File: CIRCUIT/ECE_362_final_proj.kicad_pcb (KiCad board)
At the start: 2 copper layers, 90.1 x 75.2 mm, 27 parts, among them J1 Conn_01x01_Pin, J2 Conn_01x01_Pin, J3 Conn_01x28_Socket, J4 Conn_01x28_Socket, SW2 BUTTON_MODE, SW4 BUTTON_CAPTURE, U1 TL084

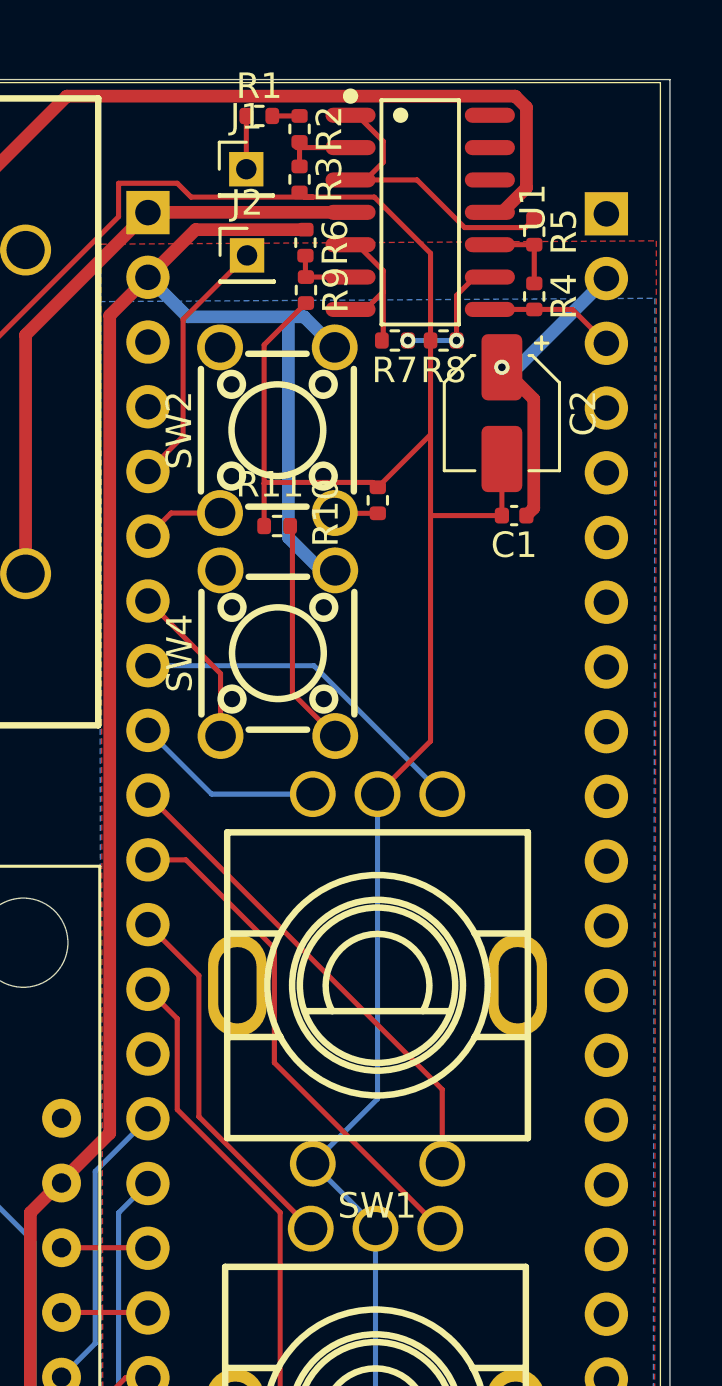
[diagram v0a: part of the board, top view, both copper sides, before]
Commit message: adjusted silkscreen
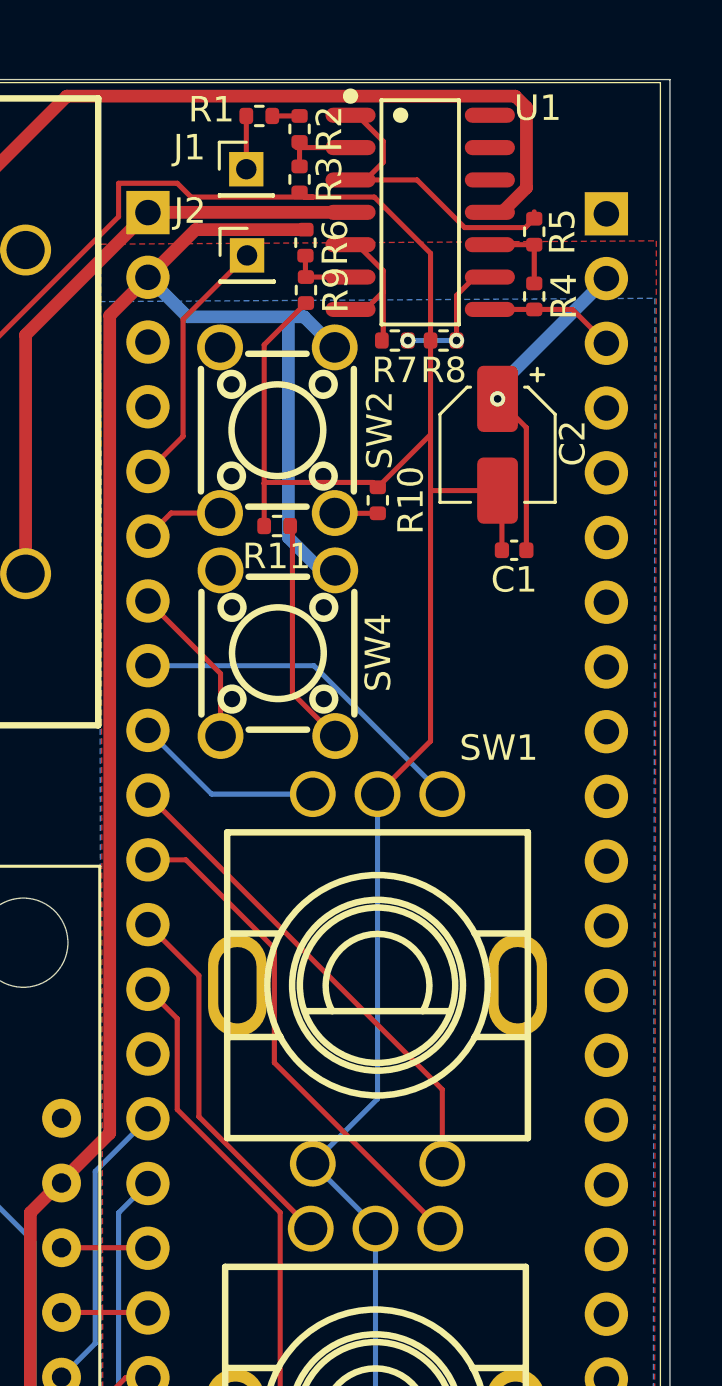
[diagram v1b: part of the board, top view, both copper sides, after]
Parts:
- moved C1 1.36 mm to (15.5, 19.7)
- moved C2 1.25 mm to (14.9, 15.6)
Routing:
- net +3.3V: track 94.1 -> 95.0 mm
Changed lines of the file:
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@@
 		(at 10.18 36.51 180)
 		(property "Reference" "SW1"
-			(at 0.014966 -8.905433 0)
+			(at -4.76 9.06 0)
 			(layer "F.SilkS")
 			(effects
@@
 		(tags "resistor")
 		(property "Reference" "R10"
-			(at -0.488 -2.038 90)
+			(at 0 1.3 90)
 			(layer "F.SilkS")
 			(effects
@@
 		(at 6.25 14.98 90)
 		(property "Reference" "SW2"
-			(at 0 -3.85 90)
+			(at 0 4.02 90)
 			(layer "F.SilkS")
 			(effects
@@
 	(footprint "Capacitor_SMD:C_0402_1005Metric"
 		(layer "F.Cu")
-		(at 15.54 18.33 180)
+		(at 15.54 19.69 180)
 		(descr "Capacitor SMD 0402 (1005 Metric), square (rectangular) end terminal, IPC_7351 nominal, (Body size source: IPC-SM-782 page 76, https://www.pcb-3d.com/wordpress/wp-content/uploads/ipc-sm-782a_amendment_1_and_2.pdf), generated with kicad-footprint-generator")
 		(tags "capacitor")
@@
 		(tags "resistor")
 		(property "Reference" "R5"
-			(at 0 -1.17 90)
+			(at 0 -1.11 270)
 			(layer "F.SilkS")
 			(effects
@@
 		(tags "resistor")
 		(property "Reference" "R11"
-			(at 0.282 1.622 0)
+			(at 0.02 -1.19 0)
 			(layer "F.SilkS")
 			(effects
@@
 		(tags "resistor")
 		(property "Reference" "R1"
-			(at 0 -1.17 0)
+			(at -1.88 -0.248375 0)
 			(layer "F.SilkS")
 			(effects
@@
 		(tags "Through hole pin header THT 1x01 2.00mm single row")
 		(property "Reference" "J1"
-			(at 0 -2.06 0)
+			(at -2.23 -0.848375 0)
 			(layer "F.SilkS")
 			(effects
@@
 		(at 6.27 23.73 90)
 		(property "Reference" "SW4"
-			(at 0 -3.85 90)
+			(at 0.02 3.94 90)
 			(layer "F.SilkS")
 			(effects
@@
 		(at 11.854 6.43 -90)
 		(property "Reference" "U1"
-			(at -0.191625 -4.41775 90)
+			(at -4.09 -4.616 180)
 			(layer "F.SilkS")
 			(effects
@@
 		(tags "Through hole pin header THT 1x01 2.00mm single row")
 		(property "Reference" "J2"
-			(at 0 -2.06 0)
+			(at -2.24 -1.74 0)
 			(layer "F.SilkS")
 			(effects
@@
 	(footprint "Capacitor_SMD:CP_Elec_4x4.5"
 		(layer "F.Cu")
-		(at 15.06 14.31 -90)
+		(at 14.89 15.55 -90)
 		(descr "SMD capacitor, aluminum electrolytic, Nichicon, 4.0x4.5mm")
 		(tags "capacitor electrolytic")
 		(property "Reference" "C2"
-			(at 0 -3.2 90)
+			(at -0.06 -2.95 90)
 			(layer "F.SilkS")
 			(effects
@@
 		(tags "Through hole socket strip THT 1x28 2.54mm single row")
 		(property "Reference" "J4"
-			(at 0 2.77 0)
+			(at 0.02 2.66 180)
 			(layer "B.SilkS")
 			(effects
@@
 	)
 	(segment
-		(start 16.02 18.33)
-		(end 16.311 18.039)
+		(start -3.443 45.683)
+		(end -2.23 44.47)
 		(width 0.5)
 		(layer "F.Cu")
@@
 	)
 	(segment
-		(start -3.443 45.683)
-		(end -2.23 44.47)
-		(width 0.5)
+		(start 16.02 14.88)
+		(end 14.89 13.75)
+		(width 0.2)
 		(layer "F.Cu")
 		(net 1)
 	)
 	(segment
-		(start 16.311 18.039)
-		(end 16.311 13.761)
-		(width 0.5)
+		(start 16.02 19.69)
+		(end 16.02 14.88)
+		(width 0.2)
 		(layer "F.Cu")
 		(net 1)
@@
 	)
 	(segment
-		(start 16.311 13.761)
-		(end 15.06 12.51)
-		(width 0.5)
-		(layer "F.Cu")
-		(net 1)
-	)
-	(segment
 		(start -3.443 61.037)
 		(end -3.443 45.683)
@@
 	)
 	(via
-		(at 15.06 12.51)
+		(at 14.89 13.75)
 		(size 0.6)
 		(drill 0.3)
@@
 	)
 	(segment
-		(start 19.16 9.03)
-		(end 15.68 12.51)
+		(start 14.89 13.3)
+		(end 14.89 13.75)
 		(width 0.5)
 		(layer "B.Cu")
@@
 	)
 	(segment
-		(start 15.68 12.51)
-		(end 15.06 12.51)
-		(width 0.2)
+		(start 19.16 9.03)
+		(end 14.89 13.3)
+		(width 0.5)
 		(layer "B.Cu")
 		(net 1)
@@
 	)
 	(segment
+		(start 12.26 17.33)
+		(end 12.26 27.18)
+		(width 0.2)
+		(layer "F.Cu")
+		(net 67)
+	)
+	(segment
+		(start 15.06 19.69)
+		(end 15.06 17.52)
+		(width 0.2)
+		(layer "F.Cu")
+		(net 67)
+	)
+	(segment
 		(start 12.26 8.037343)
 		(end 12.26 11.46)
@@
 	)
 	(segment
+		(start 14.89 17.35)
+		(end 12.28 17.35)
+		(width 0.2)
+		(layer "F.Cu")
+		(net 67)
+	)
+	(segment
 		(start -0.811 61.169)
 		(end 7.201 61.169)
@@
 	(segment
 		(start 12.26 11.46)
-		(end 12.26 27.18)
+		(end 12.26 17.33)
 		(width 0.2)
 		(layer "F.Cu")
@@
 	)
 	(segment
-		(start 15.06 18.33)
-		(end 15.06 16.11)
-		(width 0.2)
-		(layer "F.Cu")
-		(net 67)
-	)
-	(segment
-		(start 12.29 18.33)
-		(end 12.26 18.3)
-		(width 0.2)
-		(layer "F.Cu")
-		(net 67)
-	)
-	(segment
 		(start 7.12 5.648375)
 		(end 7.303125 5.8315)
@@
 		(width 0.2)
 		(layer "F.Cu")
-		(net 67)
-	)
-	(segment
-		(start 15.06 18.33)
-		(end 12.29 18.33)
-		(width 0.2)
-		(layer "F.Cu")

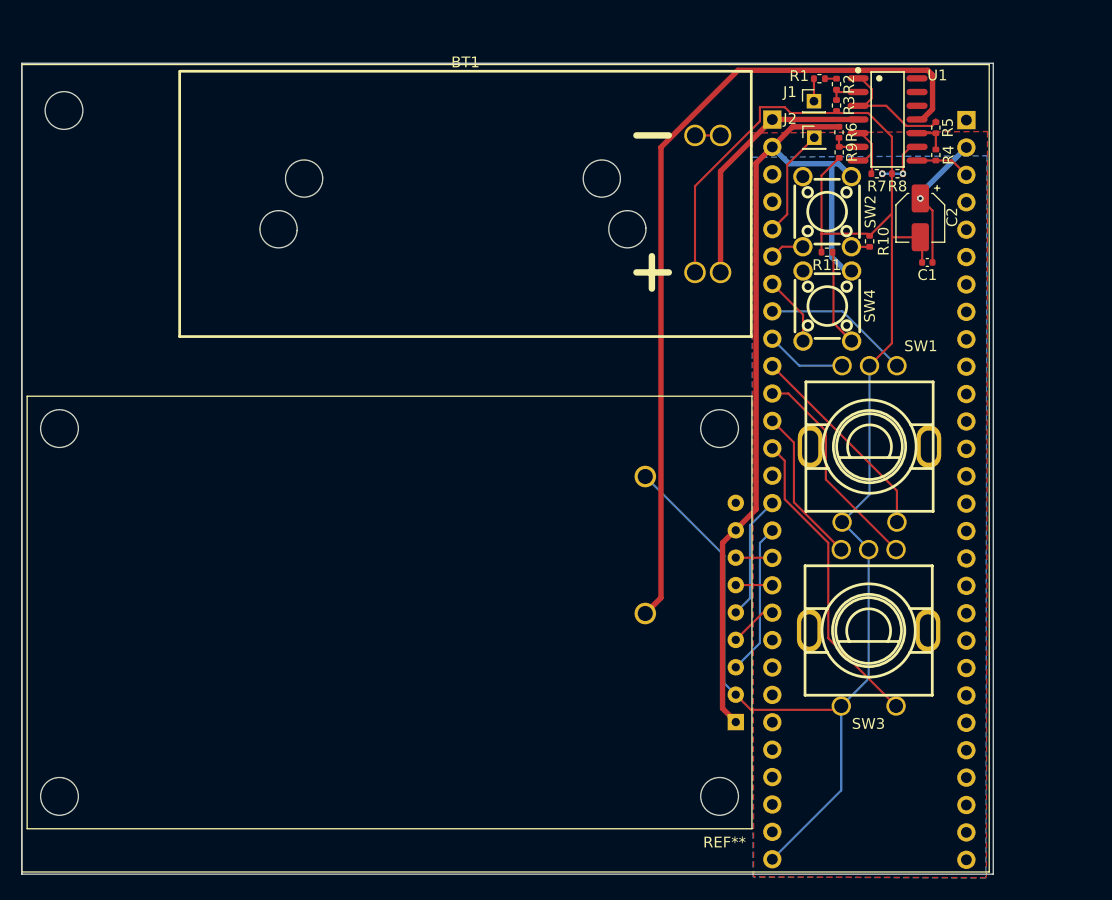
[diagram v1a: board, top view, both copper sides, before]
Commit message: adjusted signal window size
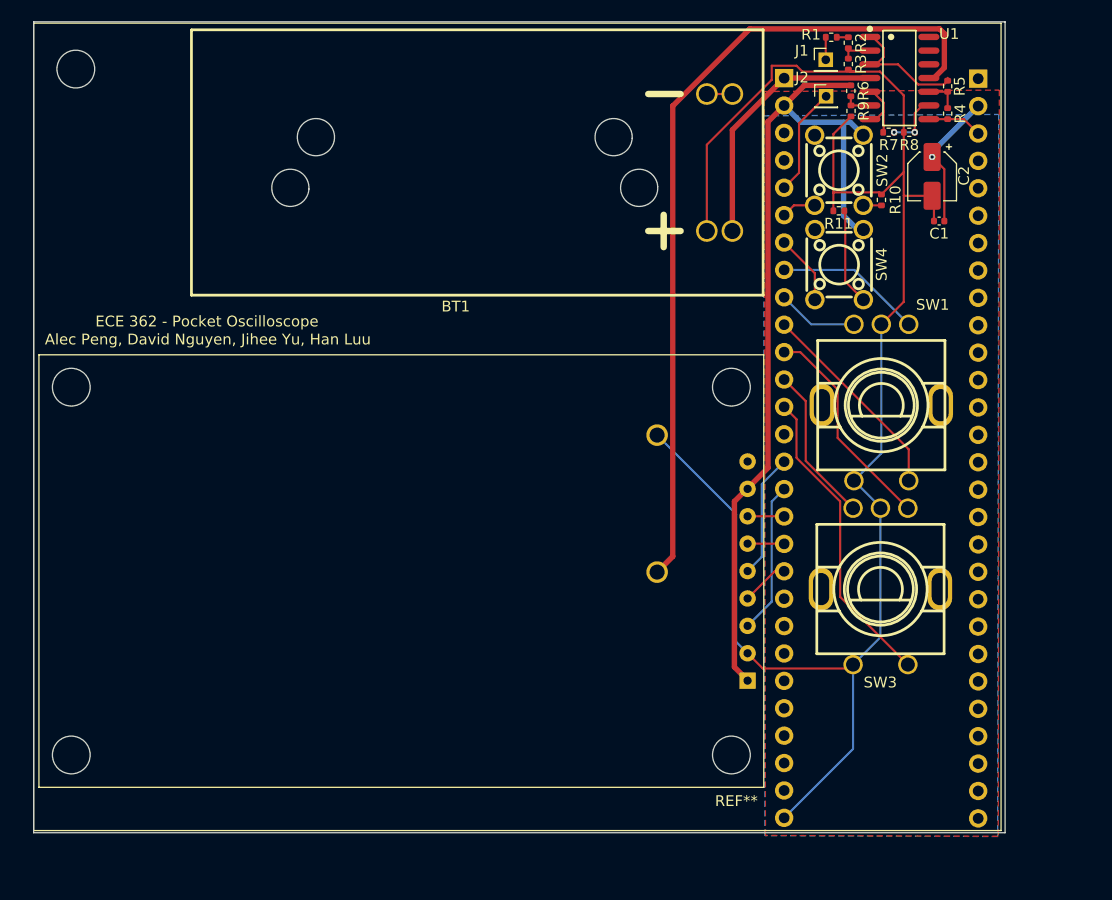
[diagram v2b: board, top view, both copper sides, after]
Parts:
- moved REF** 3.99 mm to (0.38, 68.3)
- moved SW3 3.99 mm to (11.2, 49.7)
- moved C1 3.99 mm to (16.6, 15.8)
- moved R4 3.99 mm to (17.4, 5.89)
- moved R5 3.99 mm to (17.4, 3.35)
- moved R7 3.99 mm to (12.0, 7.62)
- moved R8 3.99 mm to (13.9, 7.62)
- moved R9 3.99 mm to (8.46, 5.64)
- moved J3 3.99 mm to (2.27, 2.60)
- moved J4 3.99 mm to (20.3, 2.65)
- moved R6 3.99 mm to (8.45, 3.78)
- moved ? 3.99 mm to (-63.4, 1.76)
- moved BT1 3.99 mm to (-2.54, 10.4)
- moved BT2 3.99 mm to (-4.91, 10.4)
- moved C2 3.99 mm to (16.0, 11.7)
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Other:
- board text added: "Alec Peng, David Nguyen, Jihee Yu, Han Luu"
- board text added: "ECE 362 - Pocket Oscilloscope"

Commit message: PCB DONE
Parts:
- added U_Switch: SW-TH_SSSS222700, DPDT_switch:SW-TH_SSSS222700, F.Cu at (-0.23, 27.2)
- moved J2 8.20 mm to (14.0, 6.62)
- moved ? 8.03 mm to (-55.5, 3.41)
- moved BT2 8.03 mm to (2.96, 12.1)
- moved C2 8.03 mm to (23.8, 13.4)
- moved J1 8.03 mm to (14.0, 2.55)
- moved R1 8.03 mm to (14.5, 0.46)
- moved R10 8.03 mm to (19.1, 15.5)
- moved R2 8.03 mm to (16.1, 0.97)
- moved R3 8.03 mm to (16.1, 2.95)
- moved R4 8.03 mm to (25.3, 7.54)
- moved R5 8.03 mm to (25.3, 5.00)
- moved R6 8.03 mm to (16.3, 5.43)
- moved R9 8.03 mm to (16.3, 7.29)
- moved SW3 8.03 mm to (19.1, 51.4)
- moved SW4 8.03 mm to (15.2, 21.5)
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- gave numbers to parts that had none: 1
- renumbered REF** to U2
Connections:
- BT1 pad 2: +BATT -> BT1+
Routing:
- net GND: track 161.5 -> 183.3 mm
- net BT1+: track 0.00 -> 16.5 mm
- net +BATT: track 24.1 -> 34.8 mm
- net -BATT: track 77.1 -> 86.5 mm
- net /GPIO2: track 10.2 -> 9.48 mm
- net +3.3V: track 95.0 -> 94.5 mm, vias 1 -> 0
- net /GPIO47_ADC7: track 5.12 -> 4.66 mm, vias 0 -> 1
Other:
- board size 90.1 x 75.2 mm -> 90.5 x 76.1 mm

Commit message: final circuit
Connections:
- BATT3 pad 2: -BATT -> BAT3
- U_Switch pad 2: GND -> BT1+
- U_Switch pad 4: BT1+ -> -BATT
- U_Switch pad 5: -BATT -> BAT3
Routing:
- net -BATT: track 86.5 -> 60.4 mm
- net BAT3: track 0.00 -> 22.5 mm
- net GND: track 183.3 -> 162.9 mm
- net BT1+: track 16.5 -> 9.45 mm
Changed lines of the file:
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@@
 	(net 74 "BT1_GND")
 	(net 75 "BT1+")
+	(net 76 "BAT3")
 	(footprint "Rotary_Encoder_EC11E18244A5:SW-TH_EC11E18244A5"
 		(layer "F.Cu")
@@
 			(layers "*.Cu" "*.Mask")
 			(remove_unused_layers no)
-			(net 67 "GND")
+			(net 75 "BT1+")
 			(thermal_bridge_angle 90)
 		)
@@
 			(layers "*.Cu" "*.Mask")
 			(remove_unused_layers no)
-			(net 75 "BT1+")
+			(net 66 "-BATT")
 			(thermal_bridge_angle 90)
 		)
@@
 			(layers "*.Cu" "*.Mask")
 			(remove_unused_layers no)
-			(net 66 "-BATT")
+			(net 76 "BAT3")
 			(thermal_bridge_angle 90)
 		)
@@
 			(layers "*.Cu" "*.Mask")
 			(remove_unused_layers no)
-			(net 66 "-BATT")
+			(net 76 "BAT3")
 			(thermal_bridge_angle 90)
 		)
@@
 	)
 	(segment
-		(start -3.306892 30.1678)
-		(end -5.786307 27.688385)
-		(width 0.5)
-		(layer "F.Cu")
-		(net 66)
-	)
-	(segment
-		(start -0.228 28.8668)
-		(end 0.622 29.7168)
+		(start -3.946415 27.688385)
+		(end -2.768 28.8668)
 		(width 0.5)
 		(layer "F.Cu")
@@
 	)
 	(segment
-		(start 0.622 47.7685)
-		(end -1.6515 50.042)
-		(width 0.5)
-		(layer "F.Cu")
-		(net 66)
-	)
-	(segment
 		(start 0.6356 5.2976)
 		(end 6.2547 -0.3215)
@@
 	)
 	(segment
-		(start -1.529 30.1678)
-		(end -3.306892 30.1678)
-		(width 0.5)
-		(layer "F.Cu")
-		(net 66)
-	)
-	(segment
-		(start -0.228 28.8668)
-		(end -1.529 30.1678)
-		(width 0.5)
-		(layer "F.Cu")
-		(net 66)
-	)
-	(segment
 		(start 0.6356 6.893772)
 		(end 0.6356 5.2976)
@@
 	)
 	(segment
-		(start 0.622 29.7168)
-		(end 0.622 47.7685)
-		(width 0.5)
-		(layer "F.Cu")
-		(net 66)
-	)
-	(segment
 		(start 24.97875 0.116961)
 		(end 24.97875 3.277039)
@@
 	(segment
 		(start -5.786307 27.688385)
+		(end -3.946415 27.688385)
+		(width 0.5)
+		(layer "F.Cu")
+		(net 66)
+	)
+	(segment
+		(start -5.786307 27.688385)
 		(end -5.786307 13.315679)
 		(width 0.5)
@@
 	)
 	(segment
-		(start -0.228 25.5668)
-		(end -1.379 26.7178)
-		(width 0.2)
-		(layer "B.Cu")
-		(net 67)
-	)
-	(segment
 		(start 19.056 56.077)
 		(end 16.516 58.617)
@@
 	)
 	(segment
-		(start 2.956 18.417)
-		(end -0.228 21.601)
-		(width 0.2)
-		(layer "B.Cu")
-		(net 67)
-	)
-	(segment
 		(start 19.056 44.027)
 		(end 19.056 44.117)
@@
 	)
 	(segment
-		(start -1.379 26.7178)
-		(end -1.379 37.0695)
-		(width 0.2)
-		(layer "B.Cu")
-		(net 67)
-	)
-	(segment
 		(start -1.379 37.0695)
 		(end -1.6515 37.342)
@@
 	)
 	(segment
-		(start -0.228 21.601)
-		(end -0.228 25.5668)
-		(width 0.2)
-		(layer "B.Cu")
-		(net 67)
-	)
-	(segment
 		(start 2.956 18.417)
 		(end 2.9594 18.417)
@@
 	)
 	(segment
-		(start 5.326 18.417)
-		(end 3.875 19.868)
+		(start -0.228 23.971)
+		(end -0.228 25.5668)
 		(width 0.5)
 		(layer "F.Cu")
@@
 	)
 	(segment
-		(start -4.069 25.027908)
-		(end -4.069 27.5658)
+		(start 5.326 18.417)
+		(end -0.228 23.971)
 		(width 0.5)
 		(layer "F.Cu")
@@
 	)
 	(segment
-		(start -4.069 27.5658)
-		(end -2.768 28.8668)
+		(start -0.228 28.8668)
+		(end 0.622 29.7168)
 		(width 0.5)
 		(layer "F.Cu")
-		(net 75)
+		(net 76)
 	)
 	(segment
-		(start 1.090908 19.868)
-		(end -4.069 25.027908)
+		(start 0.622 47.7685)
+		(end -1.6515 50.042)
 		(width 0.5)
 		(layer "F.Cu")
-		(net 75)
+		(net 76)
 	)
 	(segment
-		(start 3.875 19.868)
-		(end 1.090908 19.868)
+		(start 0.622 29.7168)
+		(end 0.622 47.7685)
 		(width 0.5)
 		(layer "F.Cu")
-		(net 75)
+		(net 76)
 	)
 	(zone
